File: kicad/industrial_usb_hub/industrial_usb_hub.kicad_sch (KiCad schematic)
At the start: 0 parts

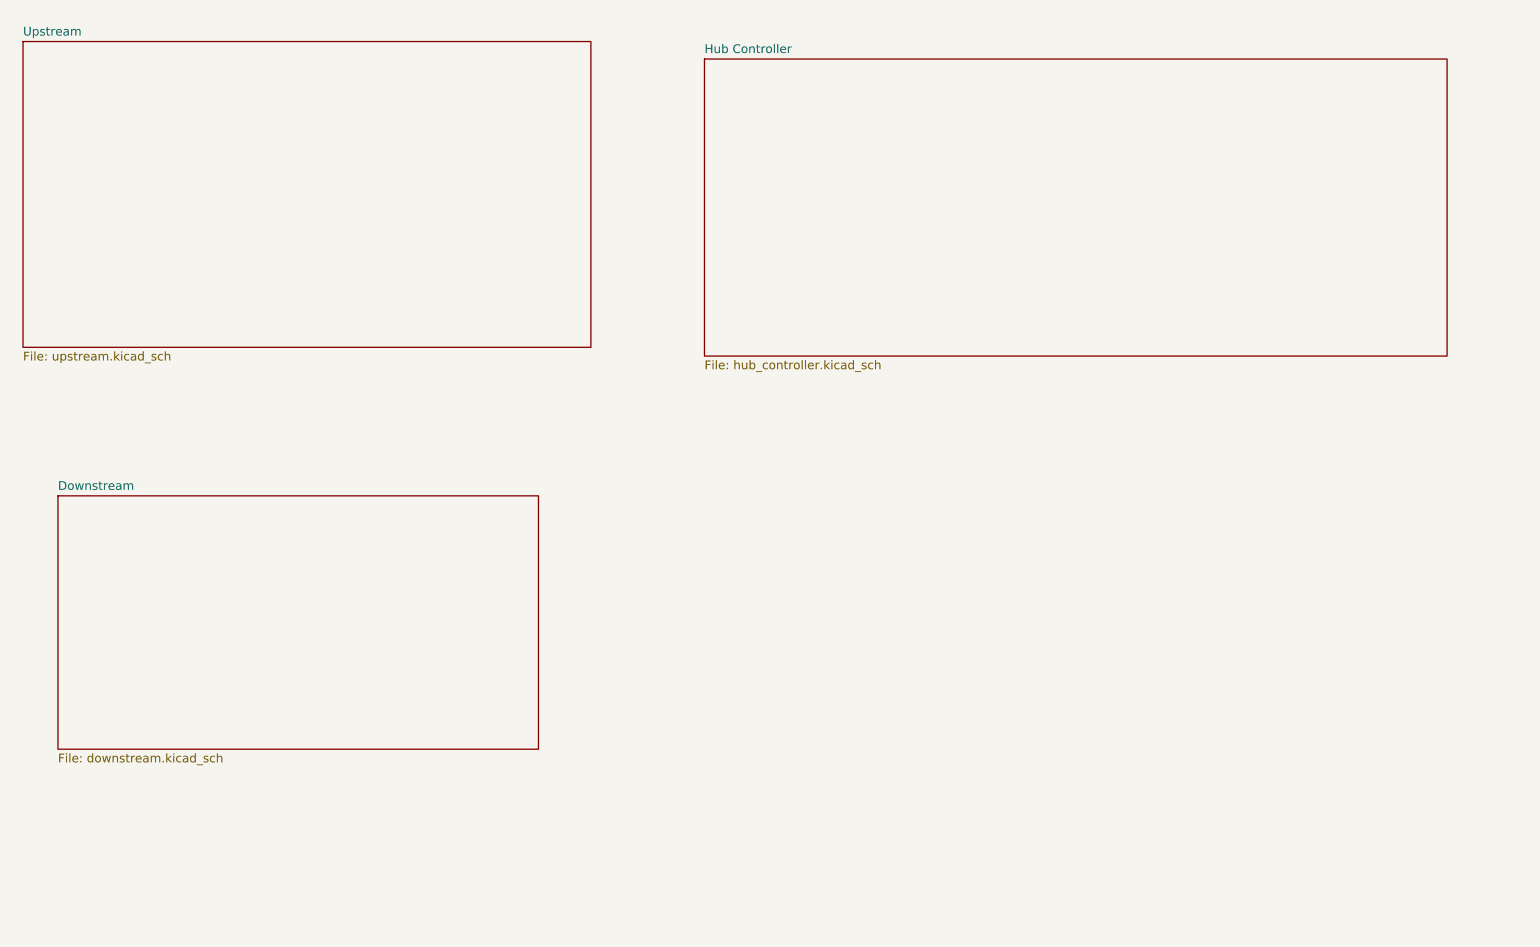
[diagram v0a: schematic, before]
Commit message: completed upstream circuit, moving on to power and downstream
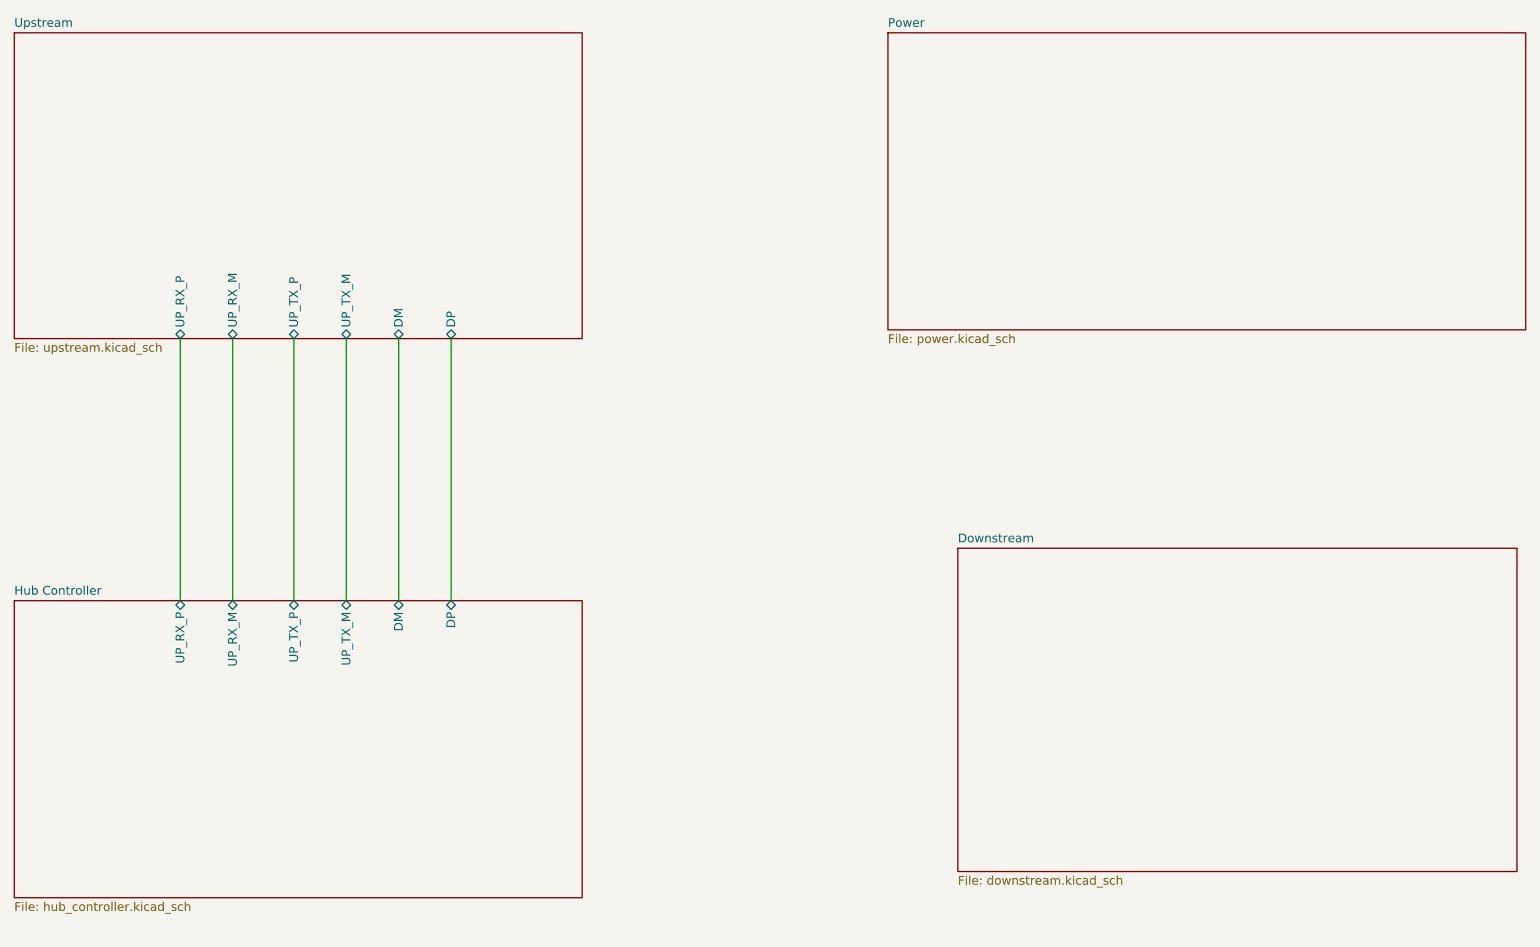
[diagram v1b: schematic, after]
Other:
- added sheet Power (power.kicad_sch)
- sheet Hub Controller ports: added DM, DP, UP_RX_M, UP_RX_P, UP_TX_M, UP_TX_P; removed none
- sheet Upstream ports: added DM, DP, UP_RX_M, UP_RX_P, UP_TX_M, UP_TX_P; removed none
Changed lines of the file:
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@@
 	(generator_version "9.0")
 	(paper "A4")
+	(wire
+		(pts
+			(xy 96.52 77.47) (xy 96.52 115.57)
+		)
+		(stroke
+			(width 0)
+			(type default)
+		)
+	)
+	(wire
+		(pts
+			(xy 88.9 77.47) (xy 88.9 115.57)
+		)
+		(stroke
+			(width 0)
+			(type default)
+		)
+	)
+	(wire
+		(pts
+			(xy 81.28 77.47) (xy 81.28 115.57)
+		)
+		(stroke
+			(width 0)
+			(type default)
+		)
+	)
+	(wire
+		(pts
+			(xy 64.77 77.47) (xy 64.77 115.57)
+		)
+		(stroke
+			(width 0)
+			(type default)
+		)
+	)
+	(wire
+		(pts
+			(xy 73.66 77.47) (xy 73.66 115.57)
+		)
+		(stroke
+			(width 0)
+			(type default)
+		)
+	)
+	(wire
+		(pts
+			(xy 57.15 77.47) (xy 57.15 115.57)
+		)
+		(stroke
+			(width 0)
+			(type default)
+		)
+	)
 	(sheet
-		(at 39.37 100.33)
-		(size 69.85 36.83)
+		(at 160.02 33.02)
+		(size 92.71 43.18)
 		(exclude_from_sim no)
 		(in_bom yes)
@@
 			(color 0 0 0 0.0000)
 		)
-		(property "Sheetname" "Downstream"
-			(at 39.37 99.6184 0)
+		(property "Sheetname" "Power"
+			(at 160.02 32.3084 0)
 			(effects
 				(font
@@
 			)
 		)
-		(property "Sheetfile" "downstream.kicad_sch"
-			(at 39.37 137.7446 0)
+		(property "Sheetfile" "power.kicad_sch"
+			(at 160.02 76.7846 0)
 			(effects
 				(font
@@
 			(project "industrial_usb_hub"
 				(path "/2bdf928d-3bff-4ef5-bf26-63be25952cbb"
-					(page "4")
+					(page "5")
 				)
 			)
@@
 	)
 	(sheet
-		(at 133.35 36.83)
-		(size 107.95 43.18)
+		(at 170.18 107.95)
+		(size 81.28 46.99)
 		(exclude_from_sim no)
 		(in_bom yes)
@@
 			(color 0 0 0 0.0000)
 		)
+		(property "Sheetname" "Downstream"
+			(at 170.18 107.2384 0)
+			(effects
+				(font
+					(size 1.27 1.27)
+				)
+				(justify left bottom)
+			)
+		)
+		(property "Sheetfile" "downstream.kicad_sch"
+			(at 170.18 155.5246 0)
+			(effects
+				(font
+					(size 1.27 1.27)
+				)
+				(justify left top)
+			)
+		)
+		(instances
+			(project "industrial_usb_hub"
+				(path "/2bdf928d-3bff-4ef5-bf26-63be25952cbb"
+					(page "4")
+				)
+			)
+		)
+	)
+	(sheet
+		(at 33.02 115.57)
+		(size 82.55 43.18)
+		(exclude_from_sim no)
+		(in_bom yes)
+		(on_board yes)
+		(dnp no)
+		(fields_autoplaced yes)
+		(stroke
+			(width 0.1524)
+			(type solid)
+		)
+		(fill
+			(color 0 0 0 0.0000)
+		)
 		(property "Sheetname" "Hub Controller"
-			(at 133.35 36.1184 0)
+			(at 33.02 114.8584 0)
 			(effects
 				(font
@@
 		)
 		(property "Sheetfile" "hub_controller.kicad_sch"
-			(at 133.35 80.5946 0)
+			(at 33.02 159.3346 0)
 			(effects
 				(font
@@
 				)
 				(justify left top)
+			)
+		)
+		(pin "UP_TX_P" bidirectional
+			(at 73.66 115.57 90)
+			(effects
+				(font
+					(size 1.27 1.27)
+				)
+				(justify right)
+			)
+		)
+		(pin "UP_RX_P" bidirectional
+			(at 57.15 115.57 90)
+			(effects
+				(font
+					(size 1.27 1.27)
+				)
+				(justify right)
+			)
+		)
+		(pin "UP_TX_M" bidirectional
+			(at 81.28 115.57 90)
+			(effects
+				(font
+					(size 1.27 1.27)
+				)
+				(justify right)
+			)
+		)
+		(pin "UP_RX_M" bidirectional
+			(at 64.77 115.57 90)
+			(effects
+				(font
+					(size 1.27 1.27)
+				)
+				(justify right)
+			)
+		)
+		(pin "DM" bidirectional
+			(at 88.9 115.57 90)
+			(effects
+				(font
+					(size 1.27 1.27)
+				)
+				(justify right)
+			)
+		)
+		(pin "DP" bidirectional
+			(at 96.52 115.57 90)
+			(effects
+				(font
+					(size 1.27 1.27)
+				)
+				(justify right)
 			)
 		)
@@
 	)
 	(sheet
-		(at 34.29 34.29)
+		(at 33.02 33.02)
 		(size 82.55 44.45)
 		(exclude_from_sim no)
@@
 		)
 		(property "Sheetname" "Upstream"
-			(at 34.29 33.5784 0)
+			(at 33.02 32.3084 0)
 			(effects
 				(font
@@
 		)
 		(property "Sheetfile" "upstream.kicad_sch"
-			(at 34.29 79.3246 0)
+			(at 33.02 78.0546 0)
 			(effects
 				(font
@@
 			)
 		)
+		(pin "UP_RX_P" bidirectional
+			(at 57.15 77.47 270)
+			(effects
+				(font
+					(size 1.27 1.27)
+				)
+				(justify left)
+			)
+		)
+		(pin "UP_RX_M" bidirectional
+			(at 64.77 77.47 270)
+			(effects
+				(font
+					(size 1.27 1.27)
+				)
+				(justify left)
+			)
+		)
+		(pin "UP_TX_P" bidirectional
+			(at 73.66 77.47 270)
+			(effects
+				(font
+					(size 1.27 1.27)
+				)
+				(justify left)
+			)
+		)
+		(pin "UP_TX_M" bidirectional
+			(at 81.28 77.47 270)
+			(effects
+				(font
+					(size 1.27 1.27)
+				)
+				(justify left)
+			)
+		)
+		(pin "DM" bidirectional
+			(at 88.9 77.47 270)
+			(effects
+				(font
+					(size 1.27 1.27)
+				)
+				(justify left)
+			)
+		)
+		(pin "DP" bidirectional
+			(at 96.52 77.47 270)
+			(effects
+				(font
+					(size 1.27 1.27)
+				)
+				(justify left)
+			)
+		)

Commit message: completed schematic
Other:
- sheet Downstream ports: added DN_D_N1, DN_D_N2, DN_D_N3, DN_D_N4, DN_D_P1, DN_D_P2, DN_D_P3, DN_D_P4, DN_RX_N1, DN_RX_N2, DN_RX_N3, DN_RX_N4, DN_RX_P1, DN_RX_P2, DN_RX_P3, DN_RX_P4, DN_TX_N1, DN_TX_N2, DN_TX_N3, DN_TX_N4, DN_TX_P1, DN_TX_P2, DN_TX_P3, DN_TX_P4, EN1, EN2, EN3, EN4, VBUS; removed none
- sheet Hub Controller ports: added DN_D_N1, DN_D_N2, DN_D_N3, DN_D_N4, DN_D_P1, DN_D_P2, DN_D_P3, DN_D_P4, DN_RX_N1, DN_RX_N2, DN_RX_N3, DN_RX_N4, DN_RX_P1, DN_RX_P2, DN_RX_P3, DN_RX_P4, DN_TX_N1, DN_TX_N2, DN_TX_N3, DN_TX_N4, DN_TX_P1, DN_TX_P2, DN_TX_P3, DN_TX_P4, PRT_CTL1, PRT_CTL2, PRT_CTL3, PRT_CTL4, UP_D_N, UP_D_P, UP_RX_N, UP_TX_N, VBUS; removed DM, DP, UP_RX_M, UP_TX_M
- sheet Power ports: added VBUS; removed none
- sheet Upstream ports: added UP_D_N, UP_D_P, UP_RX_N, UP_TX_N, VBUS; removed DM, DP, UP_RX_M, UP_TX_M
- title: (none) -> Industrial USB Hub
